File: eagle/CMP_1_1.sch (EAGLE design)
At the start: 13 parts, among them IC1 74HC85N, X1 In A, X2 In B, X3 In Cmp, X4 Out

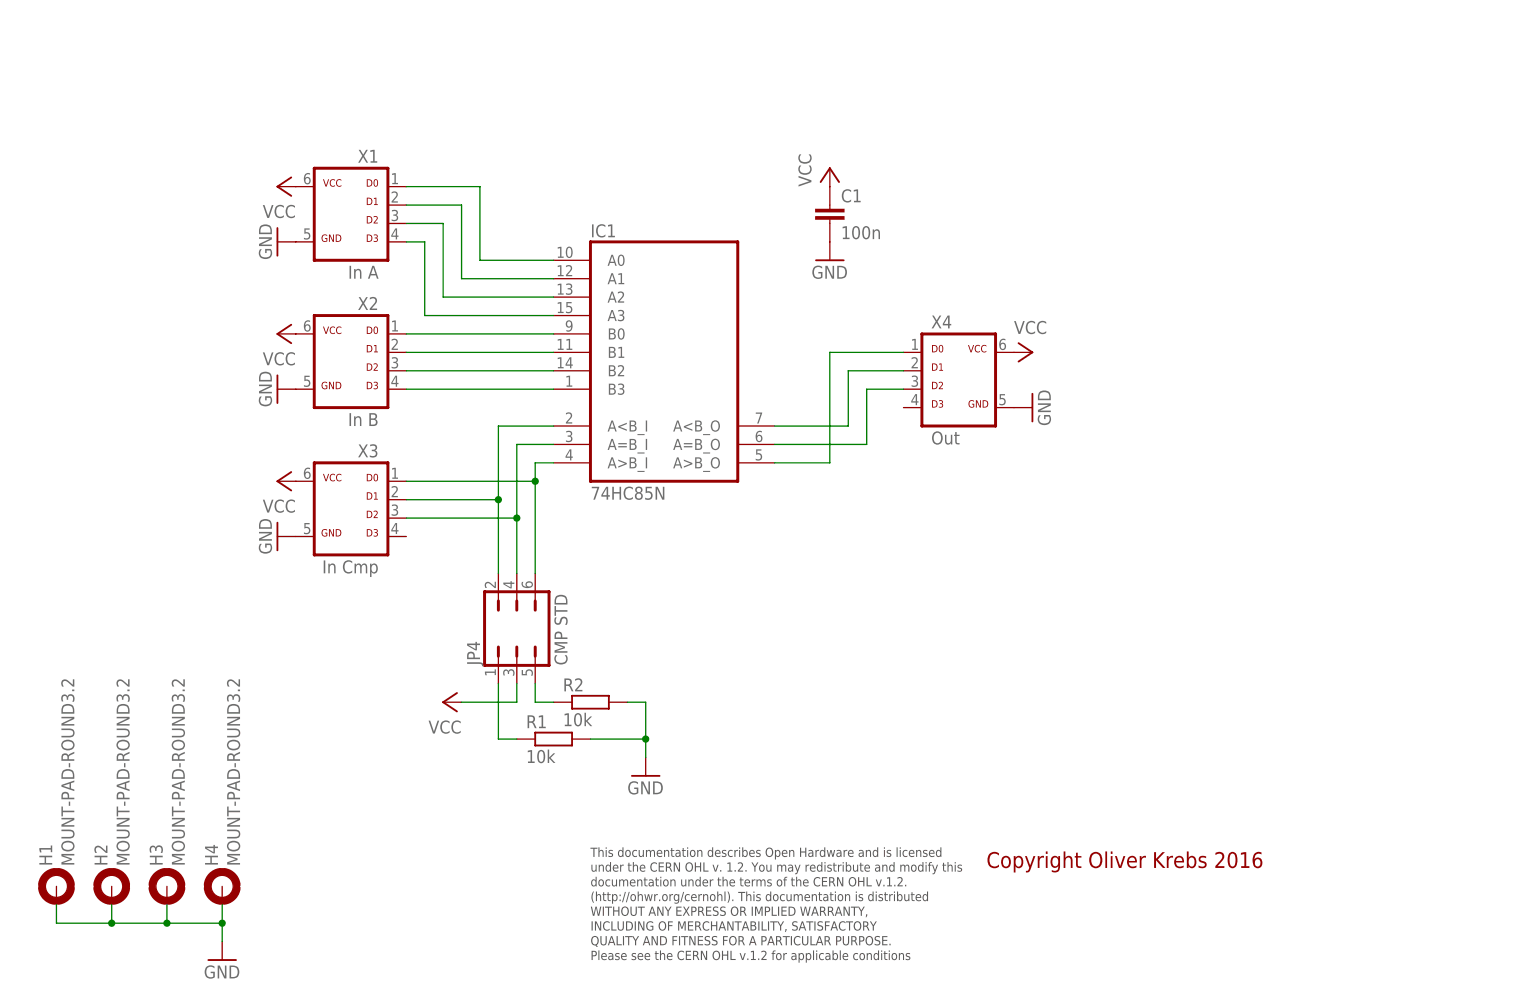
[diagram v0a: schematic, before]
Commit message: Add new tetra-Board and arduino files
Add AMP_1_0, AVC_1_0, D18_1_1, IOP_1_2, MIC_1_0, PIN_1_1, POT_1_0, PWA_1_0, PWR_1_0, RGF 2.0, SOC_2_0, VLT_1_0
Add mex_nano_shield_keyboard, mex_nano_shied_numbers

New arduino projects
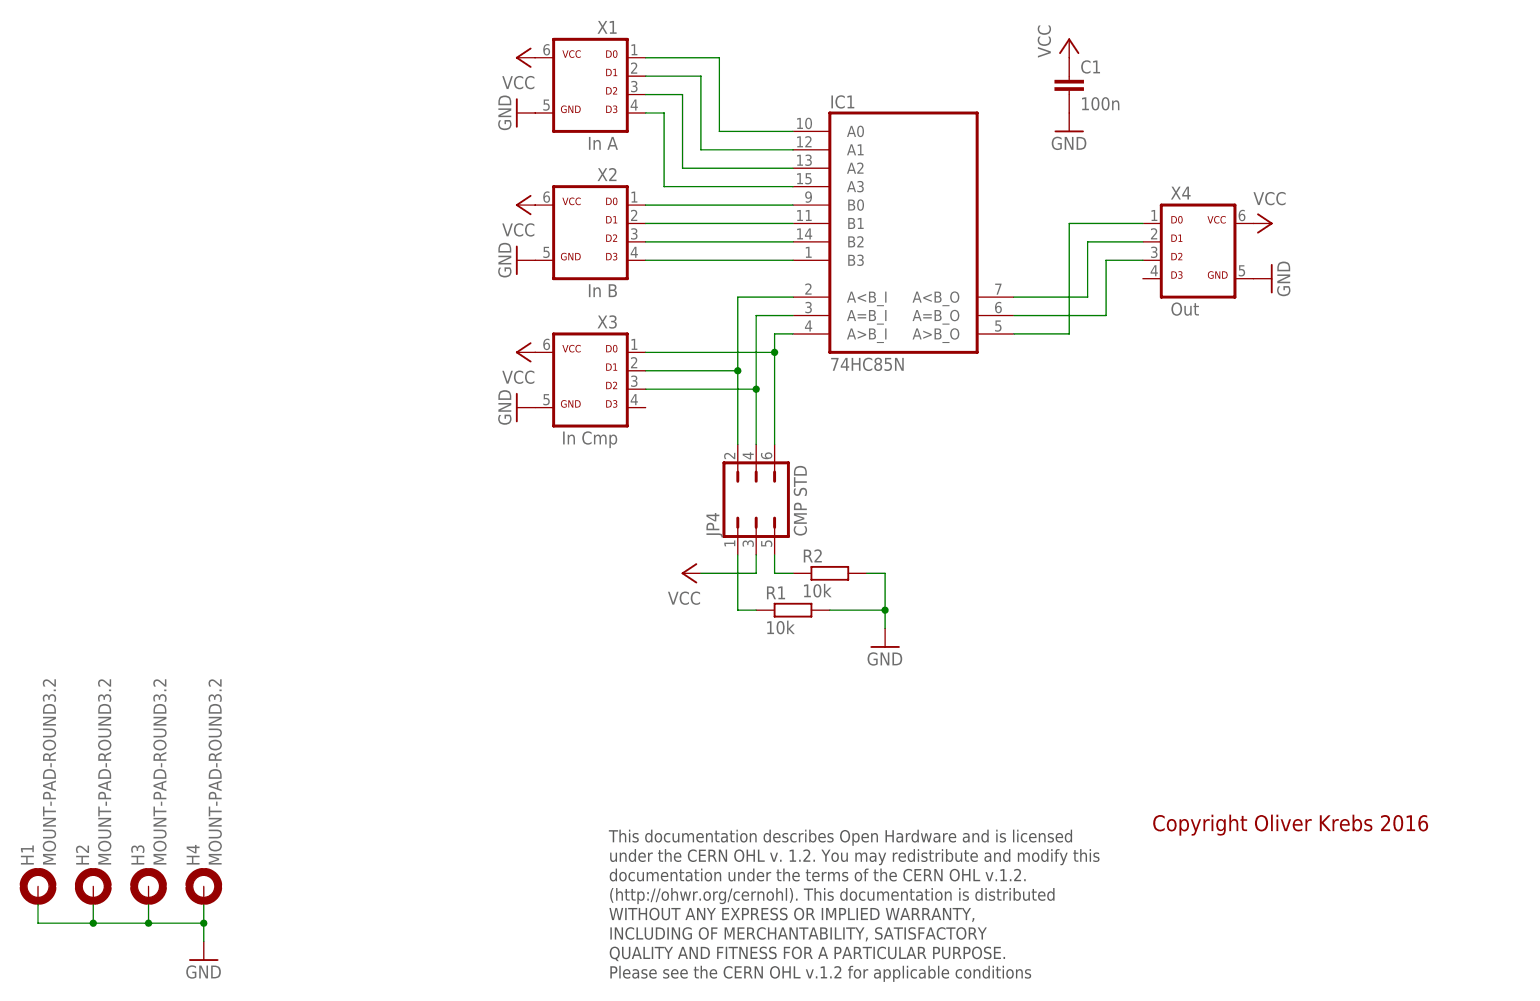
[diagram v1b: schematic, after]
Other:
- moved on the sheet: C1, H1, H2, H3, H4, IC1, JP4, R1, R2, X1, X2, X3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
